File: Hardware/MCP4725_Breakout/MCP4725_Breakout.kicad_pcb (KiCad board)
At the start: 2 copper layers, 15.6 x 15.6 mm, 37 parts, among them J1 Conn_01x02, J2 I2C, U2 MCP4725

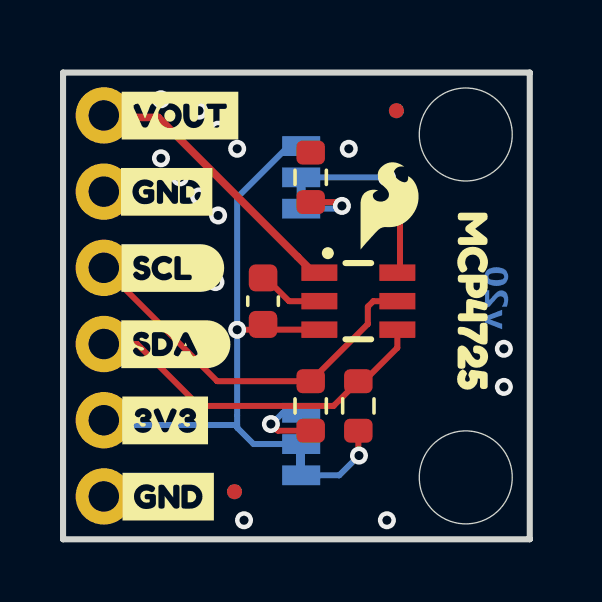
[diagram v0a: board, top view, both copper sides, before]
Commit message: Changes dual to single jumper
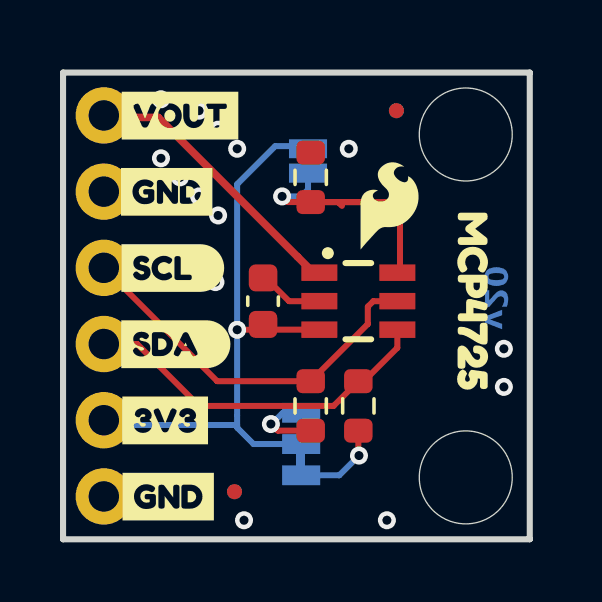
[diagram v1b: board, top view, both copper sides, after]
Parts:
- removed kibuzzard-69B9770D: G***, kibuzzard-69B9770D
- removed kibuzzard-69B97714: G***, kibuzzard-69B97714
- added kibuzzard-69BC59E1: G***, kibuzzard-69BC59E1, B.Cu at (149.1, 102.4)
- JP2: footprint SparkFun-Jumper:Jumper_3_NC-1_Trace -> SparkFun-Jumper:Jumper_2_NO
- moved Ref** 2.96 mm to (151.1, 104.5)
- moved kibuzzard-69B976CB 0.64 mm to (150.7, 99.7)
- moved JP2 0.59 mm to (149.1, 99.8)
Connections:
- JP2 pad 1: Net-(JP2-A) -> ADDR
- JP2 pad 2: ADDR -> 3.3V
- R1 pad 2: Net-(JP2-A) -> ADDR
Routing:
- net ADDR: track 6.18 -> 9.50 mm
- net Net-(JP2-A): track 2.31 -> 0.00 mm, vias 1 -> 0

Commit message: Fixes jumpers on more time
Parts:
- JP2: footprint SparkFun-Jumper:Jumper_2_NO -> SparkFun-Jumper:Jumper_2_NC_Trace
- moved JP2 0.13 mm to (149.2, 99.7), turned to -90 degrees
- turned R1 to 90 degrees
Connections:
- JP2 pad 1: ADDR -> GND
- JP2 pad 2: 3.3V -> ADDR
- R1 pad 1: GND -> ADDR
- R1 pad 2: ADDR -> 3.3V
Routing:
- net ADDR: track 9.50 -> 7.21 mm
- net 3.3V: track 20.7 -> 20.9 mm, vias 1 -> 2

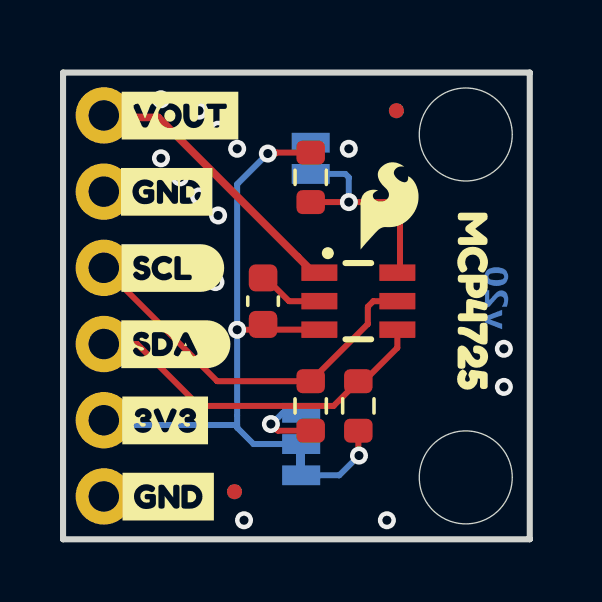
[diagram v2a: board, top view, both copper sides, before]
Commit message: Adds measures, grows small board by another 1/8 inch in X/Y direction
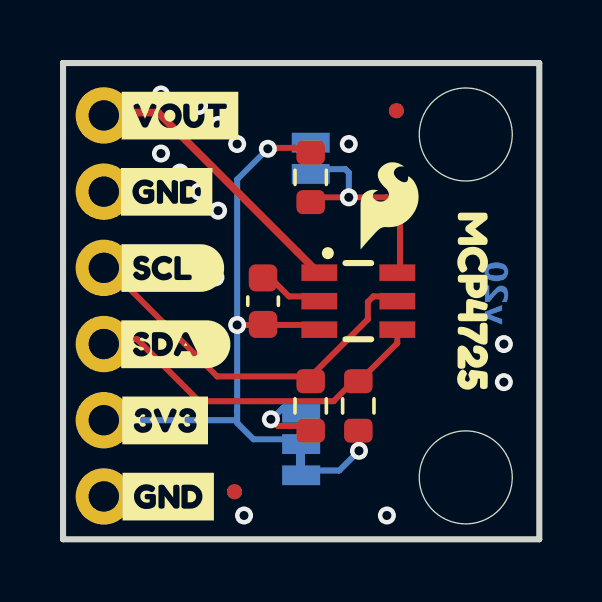
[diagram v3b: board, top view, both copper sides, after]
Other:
- board size 15.6 x 15.6 mm -> 15.9 x 15.9 mm

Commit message: Adds gerbers
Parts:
- removed kibuzzard-69BC59E1: G***, kibuzzard-69BC59E1
- moved kibuzzard-69B976CB 0.17 mm to (150.9, 99.7)
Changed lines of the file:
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@@
 	(footprint "kibuzzard-69B976CB"
 		(layer "B.Cu")
-		(at 150.7109 99.695 90)
+		(at 150.876 99.695 90)
 		(descr "Generated with KiBuzzard")
 		(tags "kb_params=eyJBbGlnbm1lbnRDaG9pY2UiOiAiTGVmdCIsICJDYXBMZWZ0Q2hvaWNlIjogIiIsICJDYXBSaWdodENob2ljZSI6ICIiLCAiRm9udENvbWJvQm94IjogIkZyZWRkeVNwYXJrLVJlZ3VsYXIiLCAiSGVpZ2h0Q3RybCI6IDAuNywgIkxheWVyQ29tYm9Cb3giOiAiRi5TaWxrUyIsICJMaW5lU3BhY2luZ0N0cmwiOiAxLjUsICJNdWx0aUxpbmVUZXh0IjogIihBRERSKSIsICJQYWRkaW5nQm90dG9tQ3RybCI6IDQuMCwgIlBhZGRpbmdMZWZ0Q3RybCI6IDEuMCwgIlBhZGRpbmdSaWdodEN0cmwiOiAxLjAsICJQYWRkaW5nVG9wQ3RybCI6IDQuMCwgIldpZHRoQ3RybCI6IDAuMCwgImFkdmFuY2VkQ2hlY2tib3giOiB0cnVlLCAiaW5saW5lRm9ybWF0VGV4dGJveCI6IHRydWUsICJsaW5lb3ZlclN0eWxlQ2hvaWNlIjogIlNxdWFyZSIsICJsaW5lb3ZlclRoaWNrbmVzc0N0cmwiOiAxfQ==")
@@
 			)
 			(stroke
-				(width 0)
-				(type solid)
-			)
-			(fill yes)
-			(layer "B.SilkS")
-		)
-		(embedded_fonts no)
-	)
-	(footprint "kibuzzard-69BC59E1"
-		(layer "B.Cu")
-		(at 149.1488 102.3874 90)
-		(descr "Generated with KiBuzzard")
-		(tags "kb_params=eyJBbGlnbm1lbnRDaG9pY2UiOiAiTGVmdCIsICJDYXBMZWZ0Q2hvaWNlIjogIiIsICJDYXBSaWdodENob2ljZSI6ICIiLCAiRm9udENvbWJvQm94IjogIkZyZWRkeVNwYXJrLVJlZ3VsYXIiLCAiSGVpZ2h0Q3RybCI6IDAuNywgIkxheWVyQ29tYm9Cb3giOiAiRi5TaWxrUyIsICJMaW5lU3BhY2luZ0N0cmwiOiAxLjUsICJNdWx0aUxpbmVUZXh0IjogIigweDYxXSIsICJQYWRkaW5nQm90dG9tQ3RybCI6IDQuMCwgIlBhZGRpbmdMZWZ0Q3RybCI6IDEuMCwgIlBhZGRpbmdSaWdodEN0cmwiOiAzLjAsICJQYWRkaW5nVG9wQ3RybCI6IDQuMCwgIldpZHRoQ3RybCI6IDAuMCwgImFkdmFuY2VkQ2hlY2tib3giOiB0cnVlLCAiaW5saW5lRm9ybWF0VGV4dGJveCI6IHRydWUsICJsaW5lb3ZlclN0eWxlQ2hvaWNlIjogIlNxdWFyZSIsICJsaW5lb3ZlclRoaWNrbmVzc0N0cmwiOiAxfQ==")
-		(property "Reference" "kibuzzard-69BC59E1"
-			(at 0 3.743827 270)
-			(layer "B.SilkS")
-			(hide yes)
-			(effects
-				(font
-					(size 0.001 0.001)
-					(thickness 0.15)
-				)
-				(justify mirror)
-			)
-		)
-		(property "Value" "G***"
-			(at 0 -3.743827 270)
-			(layer "B.SilkS")
-			(hide yes)
-			(effects
-				(font
-					(size 0.001 0.001)
-					(thickness 0.15)
-				)
-				(justify mirror)
-			)
-		)
-		(property "Datasheet" ""
-			(at 0 0 270)
-			(layer "B.Fab")
-			(hide yes)
-			(effects
-				(font
-					(size 1.27 1.27)
-					(thickness 0.15)
-				)
-				(justify mirror)
-			)
-		)
-		(property "Description" ""
-			(at 0 0 270)
-			(layer "B.Fab")
-			(hide yes)
-			(effects
-				(font
-					(size 1.27 1.27)
-					(thickness 0.15)
-				)
-				(justify mirror)
-			)
-		)
-		(attr board_only exclude_from_pos_files exclude_from_bom)
-		(fp_poly
-			(pts
-				(xy 0.700083 -0.136695) (xy 0.684061 -0.101144) (xy 0.643002 -0.087625) (xy 0.593932 -0.100644)
-				(xy 0.575906 -0.134692) (xy 0.589926 -0.176753) (xy 0.636993 -0.189771) (xy 0.685062 -0.177253)
-				(xy 0.700083 -0.136695)
-			)
-			(stroke
-				(width 0)
-				(type solid)
-			)
-			(fill yes)
-			(layer "B.SilkS")
-		)
-		(fp_poly
-			(pts
-				(xy -0.448557 -0.177754) (xy -0.406998 -0.164235) (xy -0.381462 -0.133691) (xy -0.368443 -0.088627)
-				(xy -0.362935 -0.044564) (xy -0.362434 -0.004506) (xy -0.362434 0.000501) (xy -0.367755 0.078487)
-				(xy -0.383715 0.134192) (xy -0.410315 0.167614) (xy -0.447556 0.178755) (xy -0.485235 0.167552)
-				(xy -0.512148 0.133941) (xy -0.528296 0.077924) (xy -0.533679 -0.000501) (xy -0.528359 -0.078049)
-				(xy -0.512399 -0.133441) (xy -0.485798 -0.166676) (xy -0.448557 -0.177754)
-			)
-			(stroke
-				(width 0)
-				(type solid)
-			)
-			(fill yes)
-			(layer "B.SilkS")
-		)
-		(fp_poly
-			(pts
-				(xy -0.716941 0.695827) (xy -0.800393 0.695827) (xy -0.868596 0.692477) (xy -0.936143 0.682457)
-				(xy -1.002381 0.665865) (xy -1.066675 0.642861) (xy -1.128404 0.613665) (xy -1.186974 0.578559)
-				(xy -1.241822 0.537882) (xy -1.292418 0.492024) (xy -1.338275 0.441428) (xy -1.378953 0.386581)
-				(xy -1.414058 0.328011) (xy -1.443254 0.266282) (xy -1.466259 0.201988) (xy -1.482851 0.135749)
-				(xy -1.49287 0.068203) (xy -1.496221 0) (xy -1.49287 -0.068203) (xy -1.482851 -0.135749) (xy -1.466259 -0.201988)
-				(xy -1.443254 -0.266282) (xy -1.414058 -0.328011) (xy -1.378953 -0.386581) (xy -1.338275 -0.441428)
-				(xy -1.292418 -0.492024) (xy -1.241822 -0.537882) (xy -1.186974 -0.578559) (xy -1.128404 -0.613665)
-				(xy -1.066675 -0.642861) (xy -1.002381 -0.665865) (xy -0.936143 -0.682457) (xy -0.868596 -0.692477)
-				(xy -0.800393 -0.695827) (xy -0.716941 -0.695827) (xy -0.444552 -0.695827) (xy -0.444552 -0.362017)
-				(xy -0.497878 -0.357761) (xy -0.545696 -0.344993) (xy -0.58663 -0.324589) (xy -0.619301 -0.297425)
-				(xy -0.668371 -0.23133) (xy -0.686272 -0.193777) (xy -0.698915 -0.152217) (xy -0.712935 -0.072604)
-				(xy -0.716941 0.000501) (xy -0.715689 0.042561) (xy -0.711934 0.084621) (xy -0.703797 0.129185)
-				(xy -0.689402 0.178755) (xy -0.669248 0.227575) (xy -0.643836 0.269886) (xy -0.610038 0.305812)
-				(xy -0.564723 0.335479) (xy -0.509645 0.355383) (xy -0.446555 0.362017) (xy -0.385217 0.355508)
-				(xy -0.33139 0.33598) (xy -0.286826 0.306813) (xy -0.253278 0.271388) (xy -0.227867 0.229578) (xy -0.207713 0.181259)
-				(xy -0.193193 0.131813) (xy -0.184681 0.086624) (xy -0.18055 0.043312) (xy -0.179173 -0.000501)
-				(xy -0.180675 -0.04544) (xy -0.185181 -0.090129) (xy -0.194069 -0.136195) (xy -0.208715 -0.185265)
-				(xy -0.228869 -0.232707) (xy -0.25428 -0.273891) (xy -0.287577 -0.308691) (xy -0.33139 -0.336981)
-				(xy -0.384216 -0.355758) (xy -0.444552 -0.362017) (xy -0.444552 -0.695827) (xy 0.262458 -0.695827)
-				(xy 0.262458 -0.355508) (xy 0.20037 -0.318956) (xy 0.104232 -0.221817) (xy 0.007093 -0.318956) (xy -0.054495 -0.355007)
-				(xy -0.119087 -0.318956) (xy -0.155138 -0.252861) (xy -0.119087 -0.191774) (xy -0.022949 -0.093634)
-				(xy -0.119087 0.003505) (xy -0.155639 0.065093) (xy -0.119087 0.131688) (xy -0.054995 0.16824) (xy 0.007093 0.131688)
-				(xy 0.104232 0.033548) (xy 0.20037 0.131688) (xy 0.26346 0.16774) (xy 0.32655 0.131688) (xy 0.363603 0.065594)
-				(xy 0.32655 0.003505) (xy 0.230412 -0.093634) (xy 0.32655 -0.191774) (xy 0.363603 -0.253362) (xy 0.32655 -0.318956)
-				(xy 0.262458 -0.355508) (xy 0.262458 -0.695827) (xy 0.640999 -0.695827) (xy 0.640999 -0.361016)
-				(xy 0.567839 -0.352504) (xy 0.505917 -0.326967) (xy 0.455234 -0.284406) (xy 0.41768 -0.226935) (xy 0.395148 -0.156668)
-				(xy 0.387637 -0.073605) (xy 0.391923 -0.000741) (xy 0.404782 0.066435) (xy 0.426212 0.127923) (xy 0.456215 0.183722)
-				(xy 0.49479 0.233834) (xy 0.552435 0.285533) (xy 0.618216 0.322461) (xy 0.692135 0.344617) (xy 0.774189 0.352003)
-				(xy 0.807737 0.35) (xy 0.834275 0.339986) (xy 0.855806 0.312446) (xy 0.862315 0.259871) (xy 0.855305 0.207797)
-				(xy 0.832272 0.179757) (xy 0.804733 0.170243) (xy 0.770184 0.168741) (xy 0.704214 0.16073) (xy 0.654518 0.136695)
-				(xy 0.618842 0.103147) (xy 0.594933 0.066595) (xy 0.648009 0.076609) (xy 0.708039 0.069655) (xy 0.762617 0.048792)
-				(xy 0.811743 0.01402) (xy 0.850409 -0.029987) (xy 0.873609 -0.078557) (xy 0.881342 -0.131688) (xy 0.873609 -0.192497)
-				(xy 0.850409 -0.246741) (xy 0.811743 -0.294421) (xy 0.761838 -0.331418) (xy 0.704924 -0.353616)
-				(xy 0.640999 -0.361016) (xy 0.640999 -0.695827) (xy 1.154733 -0.695827) (xy 1.154733 -0.351001)
-				(xy 1.084633 -0.330973) (xy 1.064604 -0.259871) (xy 1.064604 0.078612) (xy 1.05459 0.069599) (xy 0.993002 0.040558)
-				(xy 0.933417 0.075608) (xy 0.902372 0.141702) (xy 0.913889 0.173748) (xy 0.944433 0.207797) (xy 1.071614 0.32196)
-				(xy 1.087637 0.334979) (xy 1.155734 0.352003) (xy 1.225835 0.331474) (xy 1.245863 0.259871) (xy 1.245863 -0.260873)
-				(xy 1.225835 -0.330973) (xy 1.154733 -0.351001) (xy 1.154733 -0.695827) (xy 1.245863 -0.695827)
-				(xy 1.496221 -0.695827) (xy 1.496221 0.695827) (xy 1.245863 0.695827) (xy -0.716941 0.695827)
-			)
-			(stroke

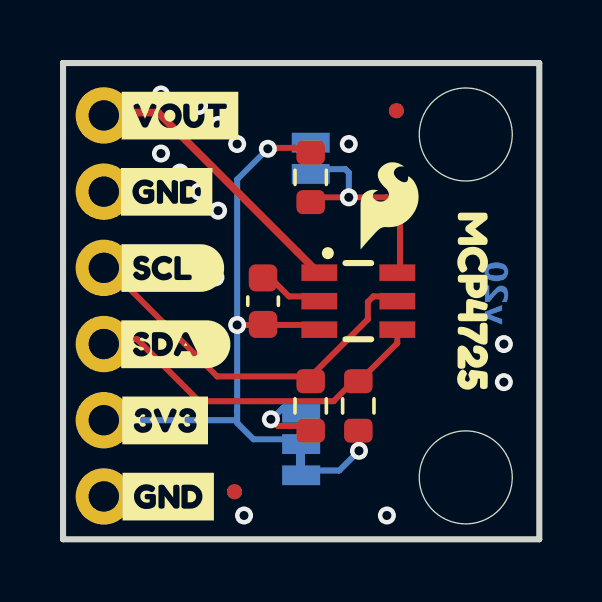
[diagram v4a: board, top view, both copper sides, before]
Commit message: Fixes trace widths
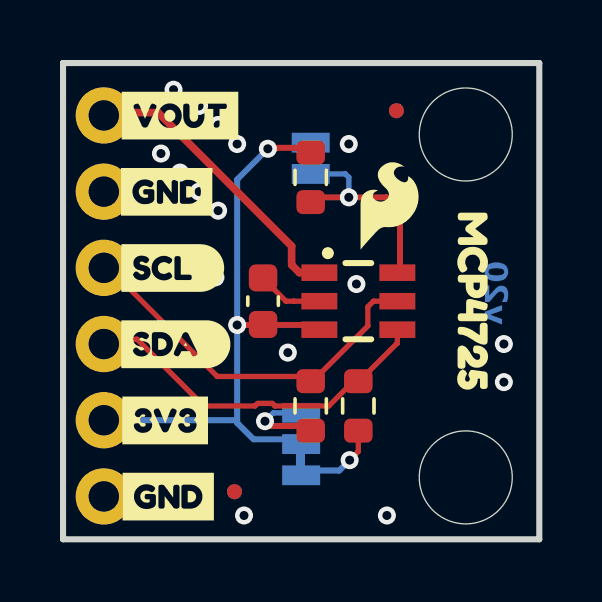
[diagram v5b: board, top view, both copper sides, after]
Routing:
- net GND: vias 14 -> 16
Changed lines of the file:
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@@
 	)
 	(segment
-		(start 149.6013 104.29875)
-		(end 148.5014 104.29875)
-		(width 0.2)
-		(layer "F.Cu")
-		(net 1)
-	)
-	(segment
-		(start 148.5014 104.29875)
-		(end 147.7264 103.52375)
-		(width 0.2)
+		(start 147.6375 103.6955)
+		(end 148.3995 104.4575)
+		(width 0.1778)
+		(layer "F.Cu")
+		(net 1)
+	)
+	(segment
+		(start 147.6375 103.6825)
+		(end 147.6375 103.6955)
+		(width 0.1778)
+		(layer "F.Cu")
+		(net 1)
+	)
+	(segment
+		(start 148.3995 104.4575)
+		(end 148.66015 104.4575)
+		(width 0.1778)
+		(layer "F.Cu")
+		(net 1)
+	)
+	(segment
+		(start 149.5124 104.4575)
+		(end 148.66015 104.4575)
+		(width 0.1778)
 		(layer "F.Cu")
 		(net 1)
@@
 	)
 	(via
-		(at 144.2339 97.56775)
+		(at 144.653 97.409)
 		(size 0.6)
 		(drill 0.3)
@@
 	)
 	(via
+		(at 150.749 103.886)
+		(size 0.6)
+		(drill 0.3)
+		(layers "F.Cu" "B.Cu")
+		(free yes)
+		(net 1)
+	)
+	(via
 		(at 151.765 111.60125)
+		(size 0.6)
+		(drill 0.3)
+		(layers "F.Cu" "B.Cu")
+		(free yes)
+		(net 1)
+	)
+	(via
+		(at 148.463 106.172)
 		(size 0.6)
 		(drill 0.3)
@@
 	)
 	(segment
-		(start 151.13 104.48125)
-		(end 151.13 105.06125)
-		(width 0.2)
+		(start 151.3205 104.4575)
+		(end 151.13 104.648)
+		(width 0.1778)
 		(layer "F.Cu")
 		(net 3)
 	)
 	(segment
-		(start 142.3289 103.1875)
+		(start 152.1125 104.4575)
+		(end 151.3205 104.4575)
+		(width 0.1778)
+		(layer "F.Cu")
+		(net 3)
+	)
+	(segment
+		(start 146.10765 106.96625)
+		(end 142.3289 103.1875)
+		(width 0.1778)
+		(layer "F.Cu")
+		(net 3)
+	)
+	(segment
+		(start 151.13 104.648)
+		(end 151.13 105.283)
+		(width 0.1778)
+		(layer "F.Cu")
+		(net 3)
+	)
+	(segment
+		(start 151.13 105.283)
+		(end 149.44675 106.96625)
+		(width 0.1778)
+		(layer "F.Cu")
+		(net 3)
+	)
+	(segment
+		(start 149.44675 106.96625)
 		(end 146.10765 106.96625)
-		(width 0.2)
+		(width 0.1778)
 		(layer "F.Cu")
 		(net 3)
 	)
 	(segment
-		(start 151.3125 104.29875)
-		(end 151.13 104.48125)
-		(width 0.2)
-		(layer "F.Cu")
-		(net 3)
-	)
-	(segment
-		(start 149.225 106.96625)
-		(end 146.10765 106.96625)
-		(width 0.2)
-		(layer "F.Cu")
-		(net 3)
-	)
-	(segment
-		(start 152.1125 104.29875)
-		(end 151.3125 104.29875)
-		(width 0.2)
-		(layer "F.Cu")
-		(net 3)
-	)
-	(segment
-		(start 151.13 105.06125)
-		(end 149.225 106.96625)
-		(width 0.2)
-		(layer "F.Cu")
-		(net 3)
+		(start 148.031771 107.95)
+		(end 147.946671 107.8649)
+		(width 0.1778)
+		(layer "F.Cu")
+		(net 4)
+	)
+	(segment
+		(start 147.370229 107.95)
+		(end 145.66265 107.95)
+		(width 0.1778)
+		(layer "F.Cu")
+		(net 4)
+	)
+	(segment
+		(start 143.44015 105.7275)
+		(end 142.3289 105.7275)
+		(width 0.1778)
+		(layer "F.Cu")
+		(net 4)
+	)
+	(segment
+		(start 145.66265 107.95)
+		(end 143.44015 105.7275)
+		(width 0.1778)
+		(layer "F.Cu")
+		(net 4)
+	)
+	(segment
+		(start 147.946671 107.8649)
+		(end 147.455329 107.8649)
+		(width 0.1778)
+		(layer "F.Cu")
+		(net 4)
 	)
 	(segment
 		(start 152.1126 105.85615)
 		(end 151.0025 106.96625)
-		(width 0.2)
+		(width 0.1778)
+		(layer "F.Cu")
+		(net 4)
+	)
+	(segment
+		(start 150.8125 106.96625)
+		(end 149.82875 107.95)
+		(width 0.1778)
 		(layer "F.Cu")
 		(net 4)
@@
 		(start 151.0025 106.96625)
 		(end 150.8125 106.96625)
-		(width 0.2)
-		(layer "F.Cu")
-		(net 4)
-	)
-	(segment
-		(start 149.9875 107.79125)
-		(end 145.5039 107.79125)
-		(width 0.2)
-		(layer "F.Cu")
-		(net 4)
-	)
-	(segment
-		(start 150.8125 106.96625)
-		(end 149.9875 107.79125)
-		(width 0.2)
+		(width 0.1778)
 		(layer "F.Cu")
 		(net 4)
@@
 		(start 152.1126 105.24875)
 		(end 152.1126 105.85615)
-		(width 0.2)
-		(layer "F.Cu")
-		(net 4)
-	)
-	(segment
-		(start 143.44015 105.7275)
-		(end 142.3289 105.7275)
-		(width 0.2)
-		(layer "F.Cu")
-		(net 4)
-	)
-	(segment
-		(start 145.5039 107.79125)
-		(end 143.44015 105.7275)
-		(width 0.2)
-		(layer "F.Cu")
-		(net 4)
-	)
-	(segment
-		(start 150.8125 109.37875)
-		(end 150.8125 108.61625)
-		(width 0.2)
+		(width 0.1778)
+		(layer "F.Cu")
+		(net 4)
+	)
+	(segment
+		(start 147.455329 107.8649)
+		(end 147.370229 107.95)
+		(width 0.1778)
+		(layer "F.Cu")
+		(net 4)
+	)
+	(segment
+		(start 149.82875 107.95)
+		(end 148.031771 107.95)
+		(width 0.1778)
+		(layer "F.Cu")
+		(net 4)
+	)
+	(segment
+		(start 150.8125 109.46765)
+		(end 150.8125 108.775)
+		(width 0.1778)
 		(layer "F.Cu")
 		(net 5)
 	)
 	(segment
-		(start 150.834725 109.445425)
-		(end 150.834725 109.400975)
-		(width 0.2)
+		(start 150.523575 109.756575)
+		(end 150.8125 109.46765)
+		(width 0.1778)
 		(layer "F.Cu")
 		(net 5)
 	)
-	(segment
-		(start 150.834725 109.400975)
-		(end 150.8125 109.37875)
-		(width 0.2)
-		(layer "F.Cu")
+	(via
+		(at 150.523575 109.756575)
+		(size 0.6)
+		(drill 0.3)
+		(layers "F.Cu" "B.Cu")
 		(net 5)
 	)
-	(via
-		(at 150.834725 109.445425)
-		(size 0.6)
-		(drill 0.3)
-		(layers "F.Cu" "B.Cu")
-		(net 5)
-	)
-	(segment
-		(start 150.834725 109.445425)
+	(segment
+		(start 150.523575 109.756575)
 		(end 150.1775 110.10265)
 		(width 0.2)
@@
 	)
 	(segment
-		(start 148.134454 108.61625)
-		(end 149.3139 108.61625)
+		(start 147.85925 108.61625)
+		(end 147.701 108.458)
 		(width 0.2)
 		(layer "F.Cu")
@@
 	)
 	(segment
-		(start 147.898454 108.39445)
-		(end 147.912654 108.39445)
+		(start 149.3139 108.61625)
+		(end 147.85925 108.61625)
 		(width 0.2)
 		(layer "F.Cu")
 		(net 6)
 	)
-	(segment
-		(start 147.912654 108.39445)
-		(end 148.134454 108.61625)
-		(width 0.2)
-		(layer "F.Cu")
+	(via
+		(at 147.701 108.458)
+		(size 0.6)
+		(drill 0.3)
+		(layers "F.Cu" "B.Cu")
 		(net 6)
 	)
-	(via
-		(at 147.898454 108.39445)
-		(size 0.6)
-		(drill 0.3)
-		(layers "F.Cu" "B.Cu")
+	(segment
+		(start 148.9075 108.1786)
+		(end 147.9804 108.1786)
+		(width 0.1778)
+		(layer "B.Cu")
 		(net 6)
 	)
 	(segment
-		(start 147.921798 108.39445)
-		(end 148.296398 108.01985)
-		(width 0.2)
+		(start 147.9804 108.1786)
+		(end 147.701 108.458)
+		(width 0.1778)
 		(layer "B.Cu")
 		(net 6)
 	)
 	(segment
-		(start 148.296398 108.01985)
-		(end 148.9964 108.01985)
-		(width 0.2)
-		(layer "B.Cu")
-		(net 6)
-	)
-	(segment
-		(start 147.898454 108.39445)
-		(end 147.921798 108.39445)
+		(start 147.701 108.458)
+		(end 147.76455 108.39445)
 		(width 0.2)
 		(layer "B.Cu")
@@
 	)
 	(segment
-		(start 150.3807 100.05695)
-		(end 150.495 100.17125)
-		(width 0.2)
-		(layer "B.Cu")
-		(net 7)
-	)
-	(segment
-		(start 150.495 100.17125)
+		(start 149.225 100.2157)
+		(end 150.3807 100.2157)
+		(width 0.1778)
+		(layer "B.Cu")
+		(net 7)
+	)
+	(segment
+		(start 150.495 100.33)
 		(end 150.495 100.99625)
-		(width 0.2)
-		(layer "B.Cu")
-		(net 7)
-	)
-	(segment
-		(start 149.225 100.05695)
-		(end 150.3807 100.05695)
-		(width 0.2)
+		(width 0.1778)
+		(layer "B.Cu")
+		(net 7)
+	)
+	(segment
+		(start 150.3807 100.2157)
+		(end 150.495 100.33)
+		(width 0.1778)
 		(layer "B.Cu")
 		(net 7)
@@
 	(segment
 		(start 144.1396 98.17195)
-		(end 148.7932 102.82555)
+		(end 142.39335 98.17195)
+		(width 0.254)
+		(layer "F.Cu")
+		(net 8)
+	)
+	(segment
+		(start 148.8465 103.5075)
+		(end 148.59 103.251)
 		(width 0.254)
 		(layer "F.Cu")
@@
 	)
 	(segment
-		(start 142.39335 98.17195)
+		(start 149.5124 103.5075)
+		(end 148.8465 103.5075)
+		(width 0.254)
+		(layer "F.Cu")
+		(net 8)
+	)
+	(segment
+		(start 148.59 102.62235)
 		(end 144.1396 98.17195)
 		(width 0.254)
@@
 	)
 	(segment
-		(start 149.3164 103.34875)
-		(end 148.7932 102.82555)
+		(start 148.59 103.251)
+		(end 148.59 102.62235)
 		(width 0.254)
 		(layer "F.Cu")
 		(net 8)
-	)
-	(segment
-		(start 148.7932 102.82555)
-		(end 148.6789 102.71125)
-		(width 0.2)
-		(layer "F.Cu")
-		(net 8)
